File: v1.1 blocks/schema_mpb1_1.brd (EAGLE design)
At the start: 126.4 x 87.6 mm, 81 parts, among them Q3 25MHz, Q4 32.768kHz, U1 NCP1117ST33T3G, U2 NCP1117ST50T3G, X1 PCI-60-POS-145167, X2 PCI-60-POS-145167, X3 PCI-60-POS-145167, X5 POWERSUPPLY_DC21MMX, X7 5566-20

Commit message: UPDATE
Updated design for Main board and I/O
- Reduced form factor, boards will be interconnected using ribbon cable connectors on 20-pin headers
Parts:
- removed H5, H6, H7, H8: MOUNT-PAD-ROUND3.2, holes:3,2-PAD
- removed J1: (no value), SparkFun-Connectors:1X03
- removed Q3: 25MHz, special:QS
- removed Q4: 32.768kHz, special:QS
- removed R16, R17, R18, R19, R20: 10K, rcl:R0805
- removed S4, S6: STS121PC04, switches:STS121PC04
- removed S5: DTS-6, switch-tact:DTS-6
- removed X1, X3: PCI-60-POS-145167, con-amp:145167-2
- removed X7: 5566-20, con-molex:5566-20
- added 3V3, B0, B1: (no value), jumper:SJ_2
- added C6: 1uF, SmartPrj:C0603-ROUND
- added C7: 100nF, SmartPrj:C0603-ROUND
- added CTS, RTS: (no value), jumper:SJ
- added F1: 500mA, adafruit:1812
- added I/O, JP3, JP4, JP5, JP6, SERIAL: (no value), pinhead-2:2X10M
- added IC1: CP2102, silabs-2:MLP28
- added JP1: (no value), pinhead:1X06
- added JTAG: (no value), pinhead-2:2X05M
- added L1: (no value), rcl:L1812
- added Q1: 8M, crystal:HC49UP
- added Q2: 32.768kHz, crystal:HC49UP
- added R4, R5: 10K, rcl:R0603
- added R7: 4k7, resistor:R0603
- added R8, R9: 10k, resistor:R0603
- added RESET: SWITCH-MOMENTARY-2SMD-1101NE, SparkFun-Electromechanical:TACTILE-SWITCH-1101NE
- added SJ1: JUMPER-PAD-3-NO, SparkFun-Passives:PAD-JUMPER-3-NO_YES_SILK_FULL_BOX_WIDE_SPACING
- C10, C11, C12, C13, C42, C43, C44, C45, C46, C47, C48, C49, C50, C51, C52, C53, C54, C55, C56, C57, C58, C59, C60, C61, C62, C63, C64, C65, C66, C67, C68, C69: device resistor:C0805 -> resistor:C0603
- R13, R14, R15, R21: device resistor:R0805 -> resistor:R0603
- X2: value PCI-60-POS-145167 -> PN61729-S; device con-amp:145167-2 -> con-berg:PN61729-S
- moved C64 341.7 mm to (124.6, -8.22)
- moved C66 340.3 mm to (42.0, 66.2), turned to 180 degrees
- moved C63 322.6 mm to (111.9, -8.22)
- moved C65 315.1 mm to (38.4, 62.7), turned to 180 degrees
- moved C68 313.4 mm to (38.4, 66.2), turned to 180 degrees
- moved C62 308.5 mm to (99.2, -8.22)
- moved C61 294.5 mm to (86.5, -8.22)
- moved C67 284.8 mm to (137.3, -8.22)
- moved C60 280.4 mm to (73.8, -8.22)
- moved C55 278.9 mm to (34.2, 65.7), turned to 180 degrees
- moved C51 268.0 mm to (46.6, 63.0)
- moved C59 266.4 mm to (61.1, -8.22)
- moved C50 253.8 mm to (46.6, 47.2)
- moved C58 252.4 mm to (48.4, -8.22)
- moved C53 250.6 mm to (20.2, 52.7), turned to 270 degrees
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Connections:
- removed net UART4_RX: U$2.24
- removed net UART4_TX: U$2.23
- removed net USART3_RX: U$2.48
- removed net USART3_TX: U$2.47
- new net N$11: IC1.2, JP1.3
- new net N$21: IC1.11, JP1.2, R9.2
- new net N$22: I/O.17
- new net N$23: I/O.19
- new net N$24: JTAG.8
- new net N$25: JTAG.10
- new net N$26: IC1.12, JP1.1
- new net N$27: IC1.28, JP1.5
- new net N$32: IC1.27, JP1.6
- new net N$41: CTS.1, IC1.24
- new net N$44: IC1.23, RTS.1
- new net N$49: I/O.18
- new net N$5: B1.2, R4.1
- new net N$50: I/O.20
- new net N$6: B0.2, R5.1
- new net N$8: IC1.9, R7.2, R8.2
- new net PA2: U$2.25
- new net PA3: U$2.26
- new net RX3: SERIAL.6, U$2.48
- new net RX4: SERIAL.8, U$2.24
- new net TX3: SERIAL.5, U$2.47
- new net TX4: SERIAL.7, U$2.23
- new net VUSB2: F1.1, SJ1.1
- net +12V: now also 3V3.3; no longer J1.1
- net +3V3: now also B0.1, B1.1, C7.1, IC1.6, JTAG.1; no longer S4.3, S6.3, X7.1, X7.2
- net +5V: now also C6.1, IC1.7, IC1.8, SJ1.2; no longer J1.3
- net BOOT0: now also R5.2; no longer R17.1
- net BOOT1: now also R4.2; no longer R16.2
- net GND: now also B0.3, B1.3, C6.2, C7.2, IC1.3, IC1.EXP, IC1.M, R8.1, R9.1, RESET.2, X2.4, X2.S1, X2.S2, X6.2; no longer R18.2, R19.2, R20.2, S4.1, S5.1, S5.2, S6.1, X6.1, X7.10, X7.12, X7.14, X7.16, X7.18, X7.20, X7.4, X7.6, X7.8
- net N$10: now also Q2.2; no longer Q4.2
- net N$12: now also Q2.1; no longer Q4.1
- net N$13: now also IC1.5, X2.2; no longer R16.1, S4.2
- net N$14: now also IC1.4, X2.3; no longer C42.2, S5.3, S5.4
- net N$15: now also JTAG.9; no longer R17.2, S6.2
- net N$17: now also L1.2, R7.1, X2.1; no longer R18.1, X7.11
- net N$18: now also F1.2, L1.1; no longer R19.1, X7.17
- net N$19: now also IC1.1, JP1.4; no longer R20.1, X7.19
- net N$45: now also 3V3.2; no longer J1.2
- net N$9: now also Q1.2; no longer Q3.2
- net NRF_SCK: now also JTAG.6; no longer X7.13
- net PE0: now also I/O.1
- net PE1: now also I/O.2
- net PE10: now also I/O.11
- net PE11: now also I/O.12
- net PE12: now also I/O.13
- net PE13: now also I/O.14
- net PE14: now also I/O.15
- net PE15: now also I/O.16
- net PE2: now also I/O.3
- net PE3: now also I/O.4
- net PE4: now also I/O.5
- net PE5: now also I/O.6
- net PE6: now also I/O.7
- net PE7: now also I/O.8
- net PE8: now also I/O.9
- net PE9: now also I/O.10
- net PH1: now also Q1.1; no longer Q3.1
- net REG_5V: now also 3V3.1, SJ1.3
- net RESET: now also C42.2, RESET.1
- net RESET#: now also JTAG.7; no longer X7.15
- net TCK/SWCLK: now also JTAG.5; no longer X7.9
- net TDI: now also JTAG.3; no longer X7.5
- net TMS/SWDIO: now also JTAG.4; no longer X7.7
- net TRST: now also JTAG.2; no longer X7.3
- net USART2_CTS: now also CTS.2
- net USART2_RTS: now also RTS.2
- net USART2_RX: now also IC1.26; no longer U$2.26
- net USART2_TX: now also IC1.25; no longer U$2.25
- net VIN: now also X6.1; no longer X6.2
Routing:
- net +12V: track 0.00 -> 58.8 mm
- net N$1: track 0.00 -> 25.9 mm
- net REG_5V: track 0.00 -> 21.5 mm
- net 3.3V: track 0.00 -> 20.6 mm, vias 0 -> 2
- net N$4: track 0.00 -> 8.57 mm
- net N$2: track 0.00 -> 5.10 mm
- net VIN: track 0.00 -> 2.59 mm, vias 0 -> 2
- net N$3: track 0.00 -> 1.67 mm
- added copper zone on layer 15, net +12V
- added copper zone on layer 15, net 3.3V
- added copper zone on layer 2, net GND
- added copper zone on layer 15, net N$1
- added copper zone on layer 1, net VIN
- added copper zone on layer 15, net VIN
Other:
- board size 126.4 x 87.6 mm -> 78.7 x 85.3 mm

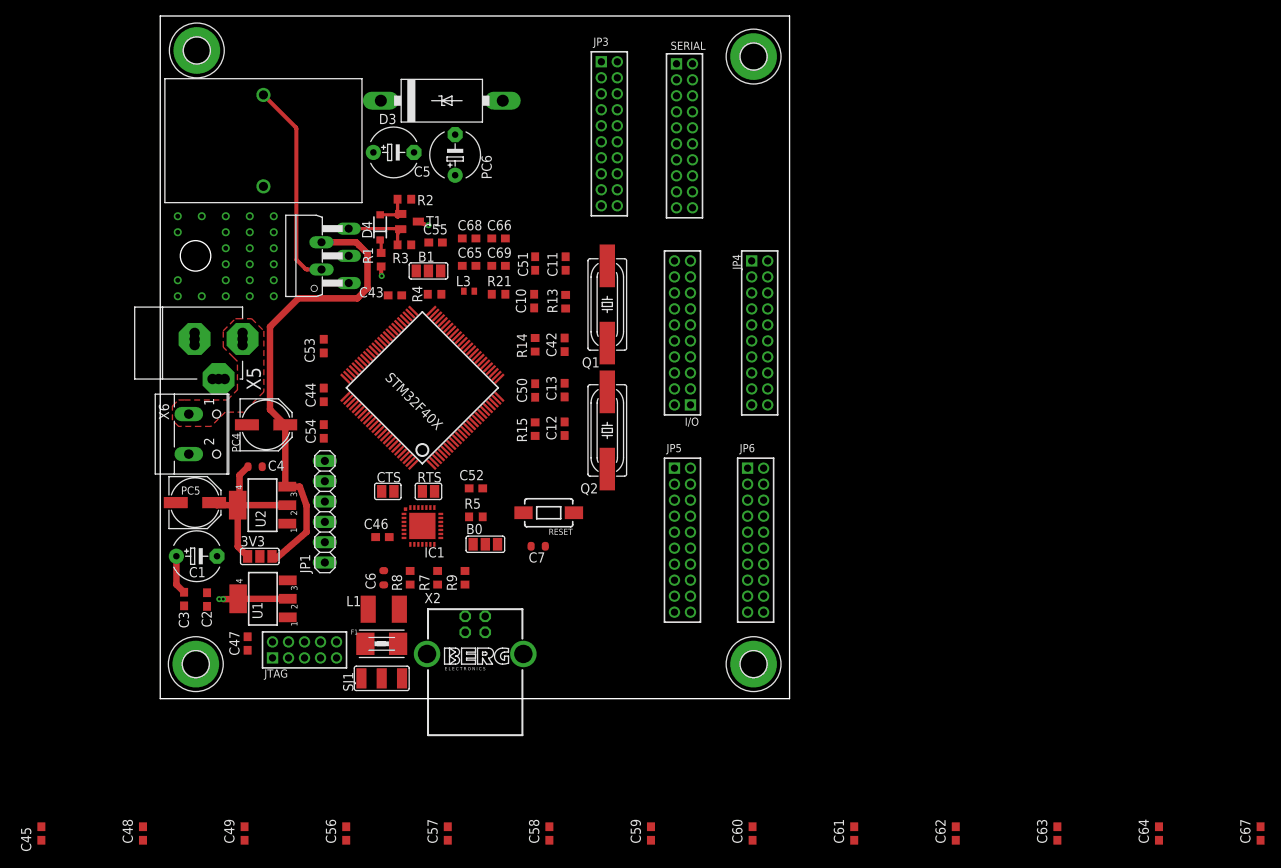
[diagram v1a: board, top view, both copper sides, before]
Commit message: Routing
First draft of routing tracks for main board
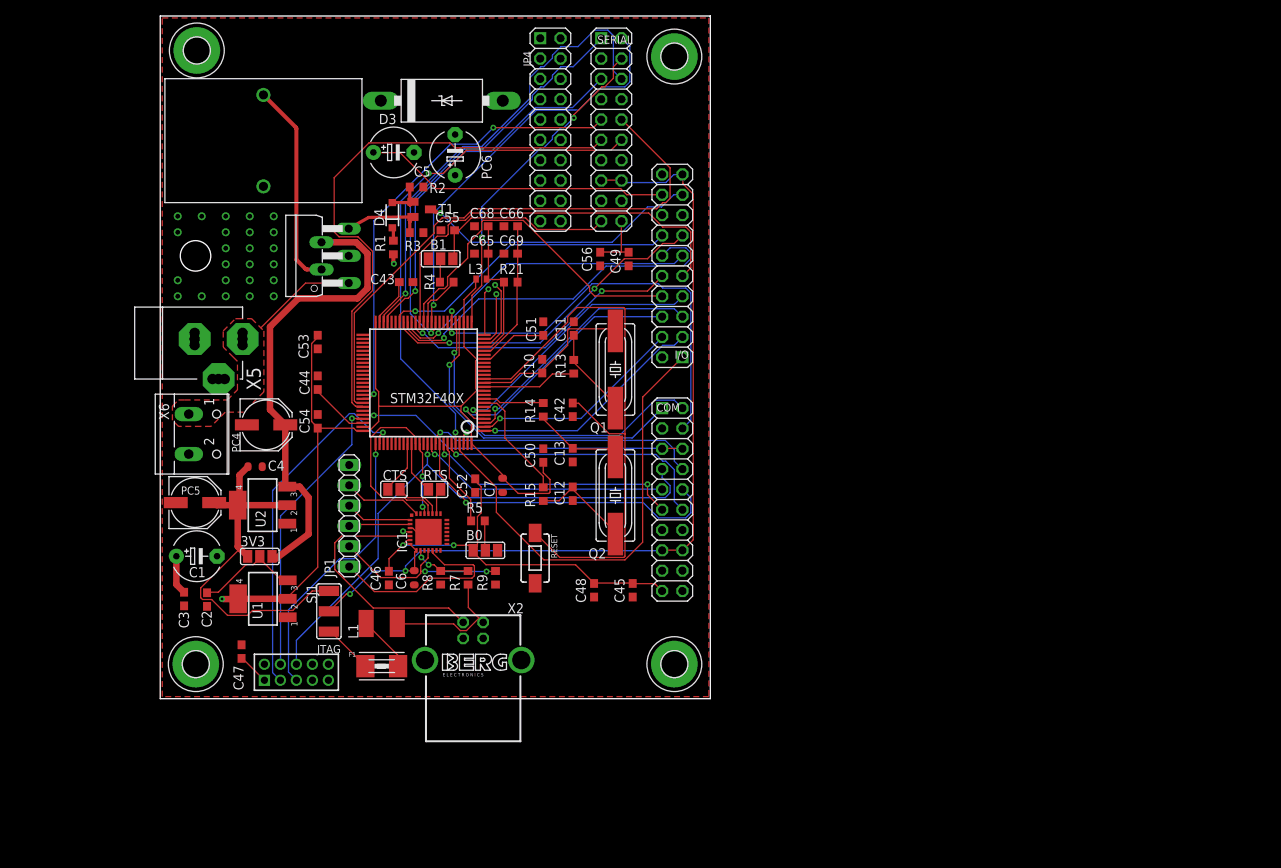
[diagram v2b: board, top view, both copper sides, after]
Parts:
- removed C57, C58, C59, C60, C61, C62, C63: 100nF, resistor:C0603
- removed C64, C67: 4.7uF, resistor:C0603
- removed JP3, JP5, JP6: (no value), pinhead-2:2X10M
- added COM: (no value), pinhead-2:2X10
- I/O, JP4, SERIAL: device pinhead-2:2X10M -> pinhead-2:2X10
- moved C49 86.4 mm to (58.3, 63.6), turned to 270 degrees
- moved C45 79.9 mm to (58.8, 22.2), turned to 270 degrees
- moved C56 78.5 mm to (54.7, 63.6), turned to 270 degrees
- moved C48 64.1 mm to (54.0, 22.2), turned to 270 degrees
- moved JP4 36.5 mm to (48.5, 79.8)
- moved SJ1 10.7 mm to (20.8, 19.6), turned to 90 degrees
- moved H3 9.91 mm to (64.0, 88.9)
- moved H4 9.91 mm to (64.0, 13.0)
- moved SERIAL 9.18 mm to (56.1, 79.8)
- moved C7 8.82 mm to (42.5, 35.3), turned to 270 degrees
- moved I/O 8.48 mm to (63.8, 62.7)
- moved C11 8.19 mm to (51.4, 54.9)
- moved Q1 8.19 mm to (56.6, 49.8)
- moved Q2 8.19 mm to (56.6, 34.0)
- moved R13 8.19 mm to (51.4, 50.1)
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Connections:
- removed net +3V3: B0.1, B1.1, C45.1, C46.1, C47.1, C48.1, C49.1, C50.1, C51.1, C52.1, C53.1, C54.1, C55.1, C56.1, C57.1, C58.1, C59.1, C60.1, C61.1, C62.1, C63.1, C64.1, C67.1, C7.1, IC1.6, JTAG.1, L3.1, U$2.100, U$2.11, U$2.19, U$2.28, U$2.50, U$2.75
- removed net N$22: I/O.17
- removed net N$23: I/O.19
- removed net N$49: I/O.18
- removed net N$50: I/O.20
- removed net PA10: U$2.69
- removed net PA2: U$2.25
- removed net PA3: U$2.26
- removed net PA8: U$2.67
- removed net PA9: U$2.68
- removed net PB9: U$2.96
- removed net R1OUT: U$2.35
- removed net T1IN: U$2.36
- new net PB12: U$2.51
- new net PB13: U$2.52
- new net PB14: U$2.53
- new net PB15: U$2.54
- new net RX1: SERIAL.2, U$2.36
- new net RX2: SERIAL.4, U$2.26
- new net RX5: SERIAL.10, U$2.68
- new net RX6: SERIAL.12, U$2.96
- new net TX1: SERIAL.1, U$2.35
- new net TX2: SERIAL.3, U$2.25
- new net TX5: SERIAL.9, U$2.67
- new net TX6: SERIAL.11, U$2.69
- net +12V: now also I/O.18
- net +5V: now also COM.15, COM.16, I/O.19, SERIAL.15, SERIAL.16
- net 3.3V: now also B0.1, B1.1, C45.1, C46.1, C47.1, C48.1, C49.1, C50.1, C51.1, C52.1, C53.1, C54.1, C55.1, C56.1, C7.1, COM.19, COM.20, I/O.20, IC1.6, JTAG.1, L3.1, SERIAL.19, SERIAL.20, U$2.100, U$2.11, U$2.19, U$2.28, U$2.50, U$2.75
- net CAN1_TX: now also COM.5, COM.6
- net ETH_MISO: now also COM.3; no longer U$2.53
- net ETH_MOSI: now also COM.4; no longer U$2.54
- net ETH_SCK: now also COM.2; no longer U$2.52
- net ETH_SS: now also COM.1; no longer U$2.51
- net GND: now also COM.13, COM.14, COM.17, COM.18, I/O.15, I/O.16, SERIAL.13, SERIAL.14, SERIAL.17, SERIAL.18; no longer C57.2, C58.2, C59.2, C60.2, C61.2, C62.2, C63.2, C64.2, C67.2
- net NRF_CE: now also COM.10
- net NRF_CS: now also COM.11
- net NRF_IRQ: now also COM.12
- net NRF_MISO: now also COM.9
- net NRF_MOSI: now also COM.8
- net NRF_SCK: now also COM.7
- net PE14: no longer I/O.15
- net PE15: no longer I/O.16
- net VIN: now also I/O.17
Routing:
- net 3.3V: track 20.6 -> 223.1 mm, vias 2 -> 3
- net +5V: track 0.00 -> 111.6 mm, vias 0 -> 2
- net RESET: track 0.00 -> 73.4 mm
- net RX5: track 0.00 -> 70.5 mm
- net NRF_SCK: track 0.00 -> 70.1 mm, vias 0 -> 1
- net TX6: track 0.00 -> 70.0 mm
- net RX6: track 0.00 -> 63.9 mm, vias 0 -> 2
- net RX3: track 0.00 -> 58.8 mm, vias 0 -> 1
- net PE0: track 0.00 -> 57.3 mm
- net TX5: track 0.00 -> 57.0 mm, vias 0 -> 2
- net PE8: track 0.00 -> 52.2 mm
- net TX1: track 0.00 -> 52.0 mm, vias 0 -> 1
- net ETH_MOSI: track 0.00 -> 51.9 mm, vias 0 -> 1
- net RX1: track 0.00 -> 50.9 mm, vias 0 -> 1
- net VIN: track 2.59 -> 50.1 mm
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- added copper zone on layer 1, net GND
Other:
- board size 78.7 x 85.3 mm -> 68.8 x 85.3 mm

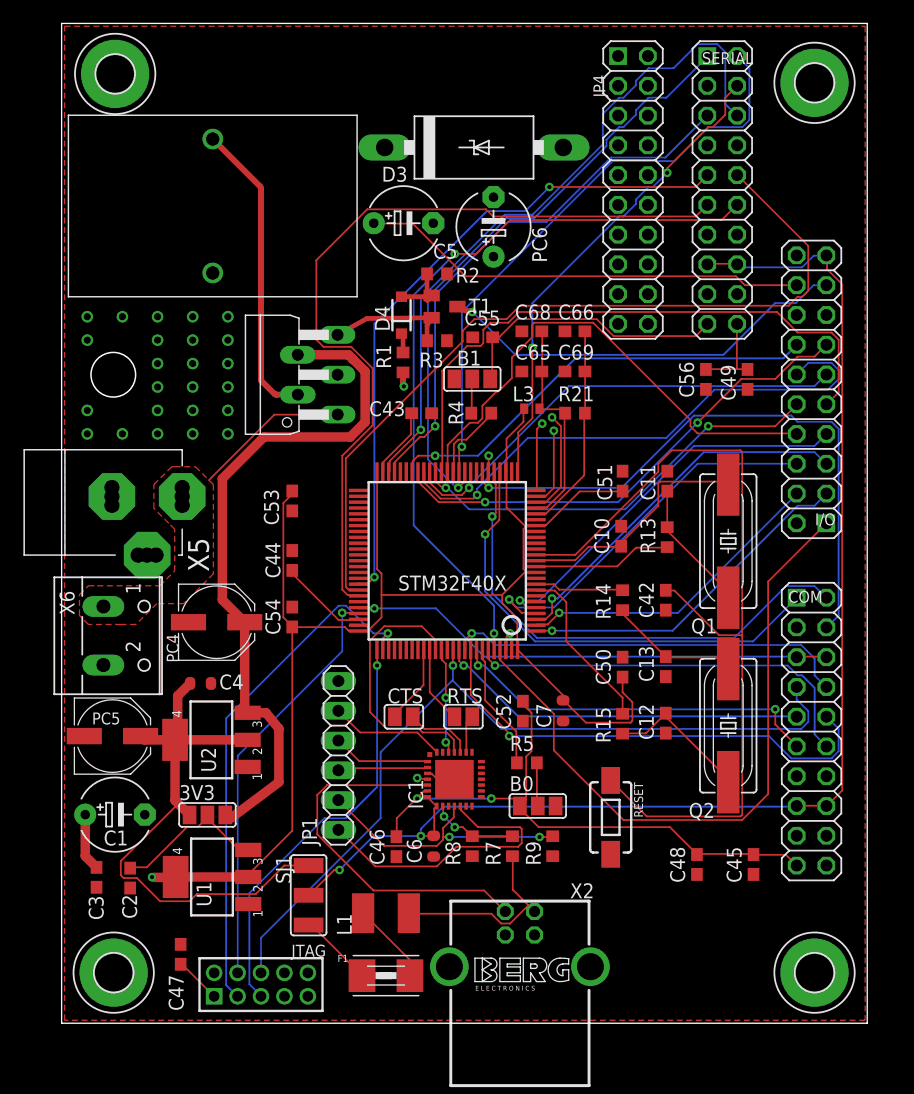
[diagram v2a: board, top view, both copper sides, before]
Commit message: Power Tracks
Routed main power tracks for Main board PCB
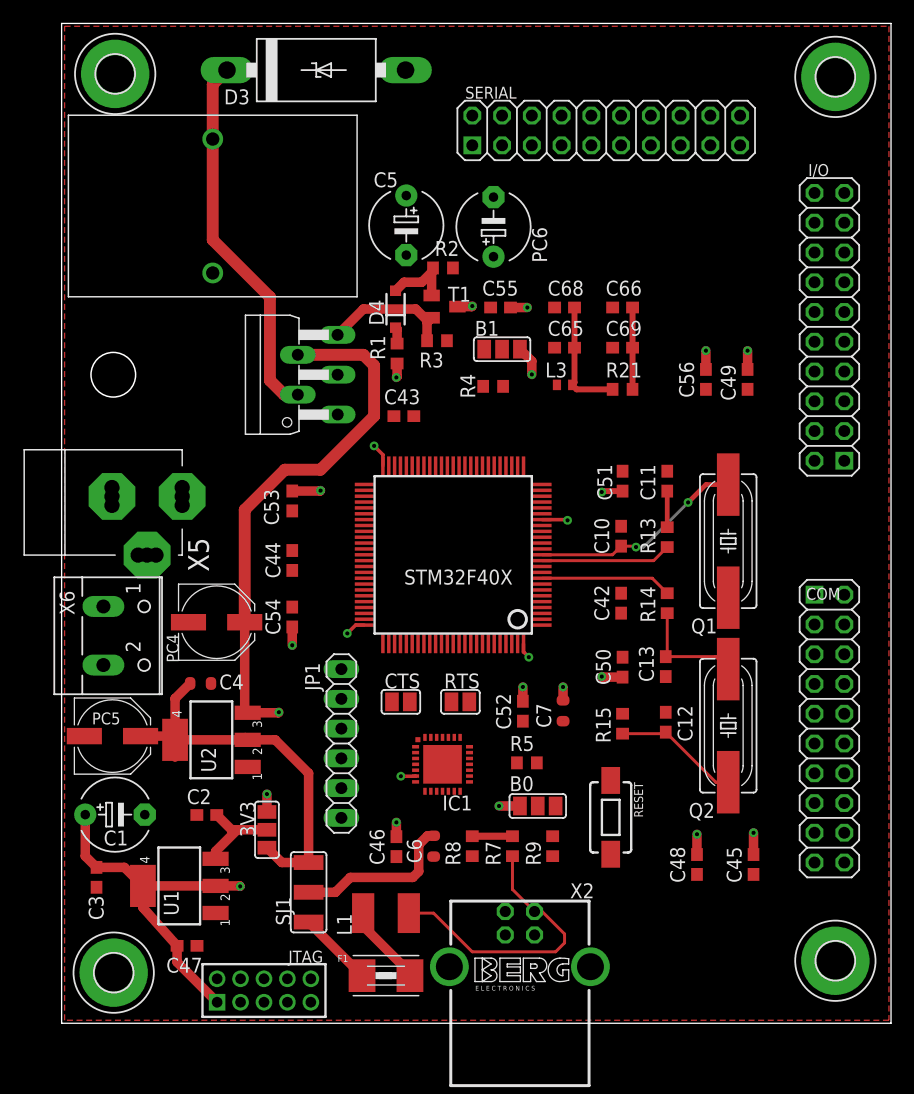
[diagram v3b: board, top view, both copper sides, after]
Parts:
- removed JP4: (no value), pinhead-2:2X10
- moved D3 15.0 mm to (21.5, 90.0)
- moved SERIAL 11.1 mm to (46.2, 84.8), turned to 0 degrees
- moved C2 8.47 mm to (12.1, 26.4), turned to 180 degrees
- moved I/O 5.55 mm to (65.3, 68.1)
- moved 3V3 5.24 mm to (17.3, 25.1), turned to 90 degrees
- moved C66 4.54 mm to (47.6, 69.7)
- moved C69 4.54 mm to (47.6, 66.3)
- moved R21 4.54 mm to (47.6, 62.7)
- moved C42 3.82 mm to (47.5, 44.5)
- moved R14 3.82 mm to (51.4, 44.5)
- moved B1 3.59 mm to (37.3, 66.2)
- moved C65 3.45 mm to (42.7, 66.3)
- moved C68 3.45 mm to (42.7, 69.7)
- moved L3 3.45 mm to (42.7, 63.1)
- moved C55 2.96 mm to (37.2, 69.7)
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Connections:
- removed net PB14: U$2.53
- removed net PB15: U$2.54
- new net USB_OTG_HS_DM: COM.13, U$2.53
- new net USB_OTG_HS_DP: COM.14, U$2.54
- net +12V: now also I/O.20; no longer I/O.18
- net 3.3V: now also I/O.17; no longer I/O.20
- net GND: no longer COM.13, COM.14
- net VIN: now also I/O.18; no longer I/O.17
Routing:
- net 3.3V: track 223.1 -> 63.7 mm, vias 3 -> 20
- net +5V: track 111.6 -> 14.0 mm, vias 2 -> 0
- net RESET: track 73.4 -> 0.00 mm
- net RX5: track 70.5 -> 0.00 mm
- net NRF_SCK: track 70.1 -> 0.00 mm, vias 1 -> 0
- net TX6: track 70.0 -> 0.00 mm
- net RX6: track 63.9 -> 0.00 mm, vias 2 -> 0
- net RX3: track 58.8 -> 0.00 mm, vias 1 -> 0
- net PE0: track 57.3 -> 0.00 mm
- net TX5: track 57.0 -> 0.00 mm, vias 2 -> 0
- net PE8: track 52.2 -> 0.00 mm
- net TX1: track 52.0 -> 0.00 mm, vias 1 -> 0
- net ETH_MOSI: track 51.9 -> 0.00 mm, vias 1 -> 0
- net RX1: track 50.9 -> 0.00 mm, vias 1 -> 0
- net PE11: track 46.4 -> 0.00 mm, vias 1 -> 0
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- removed copper zone on layer 15, net +12V
- removed copper zone on layer 15, net N$1
- removed copper zone on layer 1, net VIN
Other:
- board size 68.8 x 85.3 mm -> 70.8 x 85.3 mm

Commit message: Board dimensions
Added board dimensions
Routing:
- net VREF+: track 6.98 -> 25.6 mm
- net VDDA: track 10.3 -> 23.4 mm
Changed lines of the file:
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@@
 <wire x1="70.536" y1="93.97" x2="-0.254" y2="93.97" width="0" layer="20"/>
 <wire x1="-0.254" y1="93.97" x2="-0.254" y2="8.636" width="0" layer="20"/>
+<dimension x1="-0.254" y1="8.128" x2="70.612" y2="8.128" x3="35.179" y3="-0.254" textsize="1.778" layer="21"/>
+<dimension x1="72.136" y1="8.382" x2="71.882" y2="93.726" x3="74.8014625" y3="51.062309375" textsize="1.778" layer="21"/>
 </plain>
 <attributes>
@@
 <wire x1="43.322" y1="63.119" x2="43.703" y2="62.738" width="0.508" layer="1"/>
 <wire x1="43.703" y1="62.738" x2="46.775" y2="62.738" width="0.508" layer="1"/>
-<wire x1="40.76878125" y1="53.119203125" x2="43.703" y2="62.738" width="0" layer="19" extent="1-1"/>
+<wire x1="46.775" y1="62.738" x2="46.775" y2="57.443" width="0.254" layer="1"/>
+<wire x1="46.775" y1="57.443" x2="42.418" y2="53.086" width="0.254" layer="1"/>
+<wire x1="42.418" y1="53.086" x2="42.384796875" y2="53.119203125" width="0.254" layer="1"/>
+<wire x1="42.384796875" y1="53.119203125" x2="40.76878125" y2="53.119203125" width="0.254" layer="1"/>
 </signal>
 <signal name="N$16">
@@
 <wire x1="48.475" y1="62.738" x2="48.475" y2="66.294" width="0.508" layer="1"/>
 <wire x1="48.475" y1="66.294" x2="48.475" y2="69.723" width="0.508" layer="1"/>
-<wire x1="40.76878125" y1="52.619203125" x2="48.475" y2="62.738" width="0" layer="19" extent="1-1"/>
+<wire x1="48.475" y1="62.738" x2="49.53" y2="61.683" width="0.254" layer="1"/>
+<wire x1="49.53" y1="61.683" x2="49.53" y2="53.848" width="0.254" layer="1"/>
+<wire x1="49.53" y1="53.848" x2="48.26" y2="52.578" width="0.254" layer="1"/>
+<wire x1="48.26" y1="52.578" x2="41.656" y2="52.578" width="0.254" layer="1"/>
+<wire x1="41.656" y1="52.578" x2="41.614796875" y2="52.619203125" width="0.254" layer="1"/>
+<wire x1="41.614796875" y1="52.619203125" x2="40.76878125" y2="52.619203125" width="0.254" layer="1"/>
 </signal>
 <signal name="USART2_TX">
